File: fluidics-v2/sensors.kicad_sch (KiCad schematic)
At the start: 16 parts, among them IC6 HSCMAND060PA3A3, IC8 HSCMAND060PA3A3, J5 0533980671, U7 LTC4316CMS-TRPBF

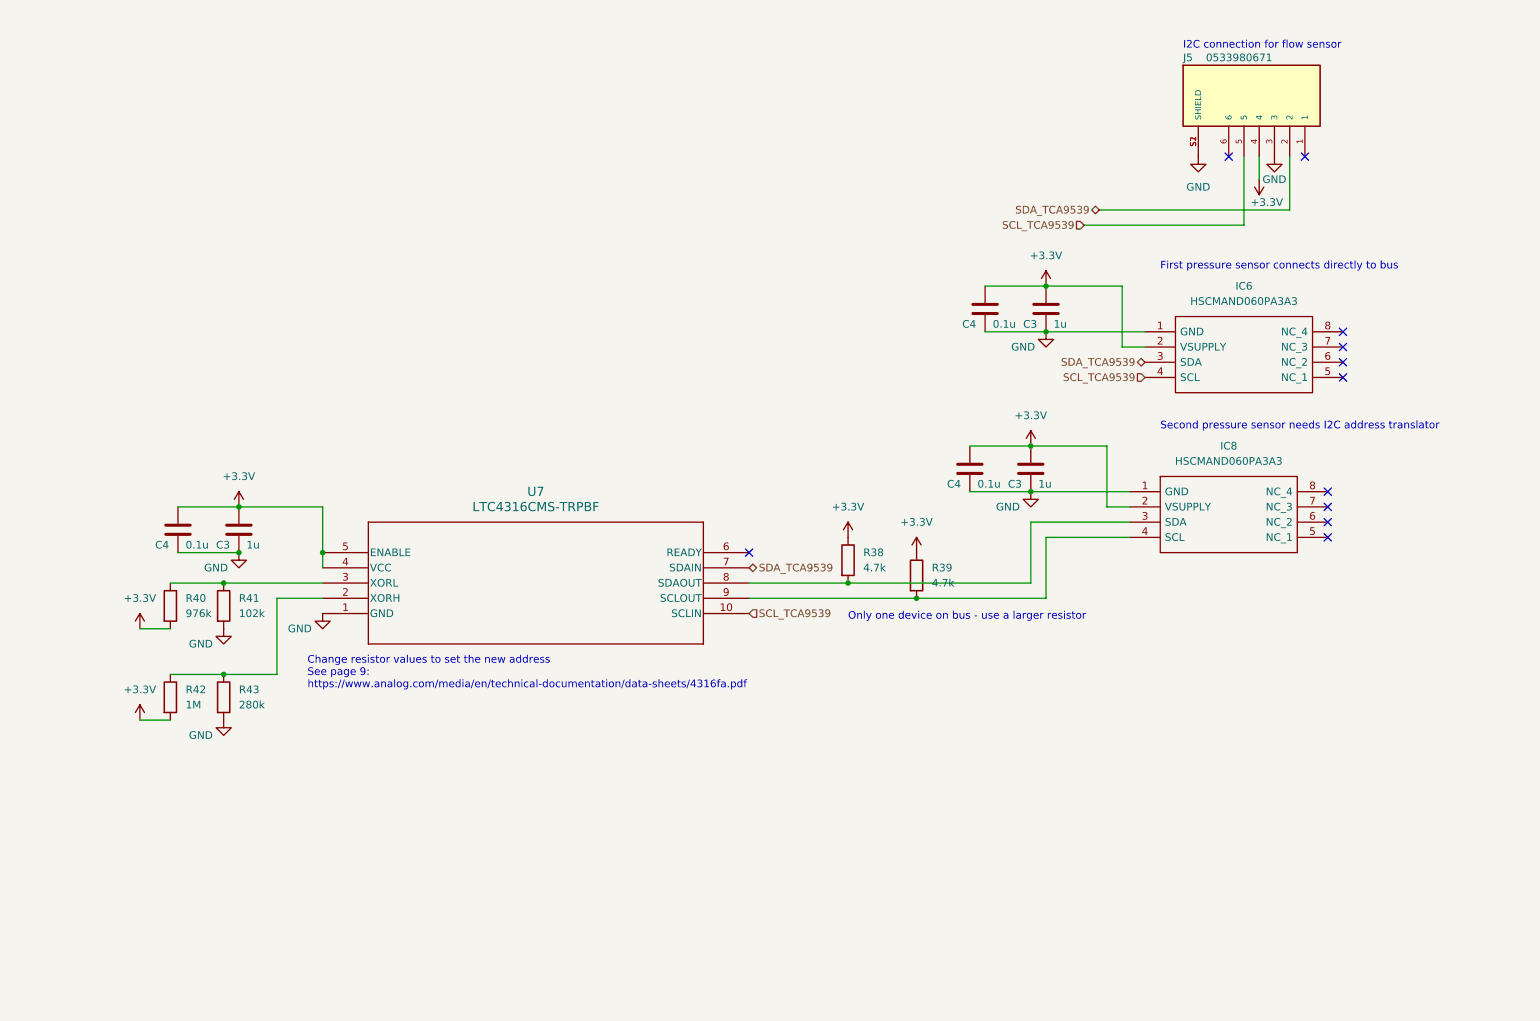
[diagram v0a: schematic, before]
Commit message: added footprints and mounting holes, cleaned up some sheets
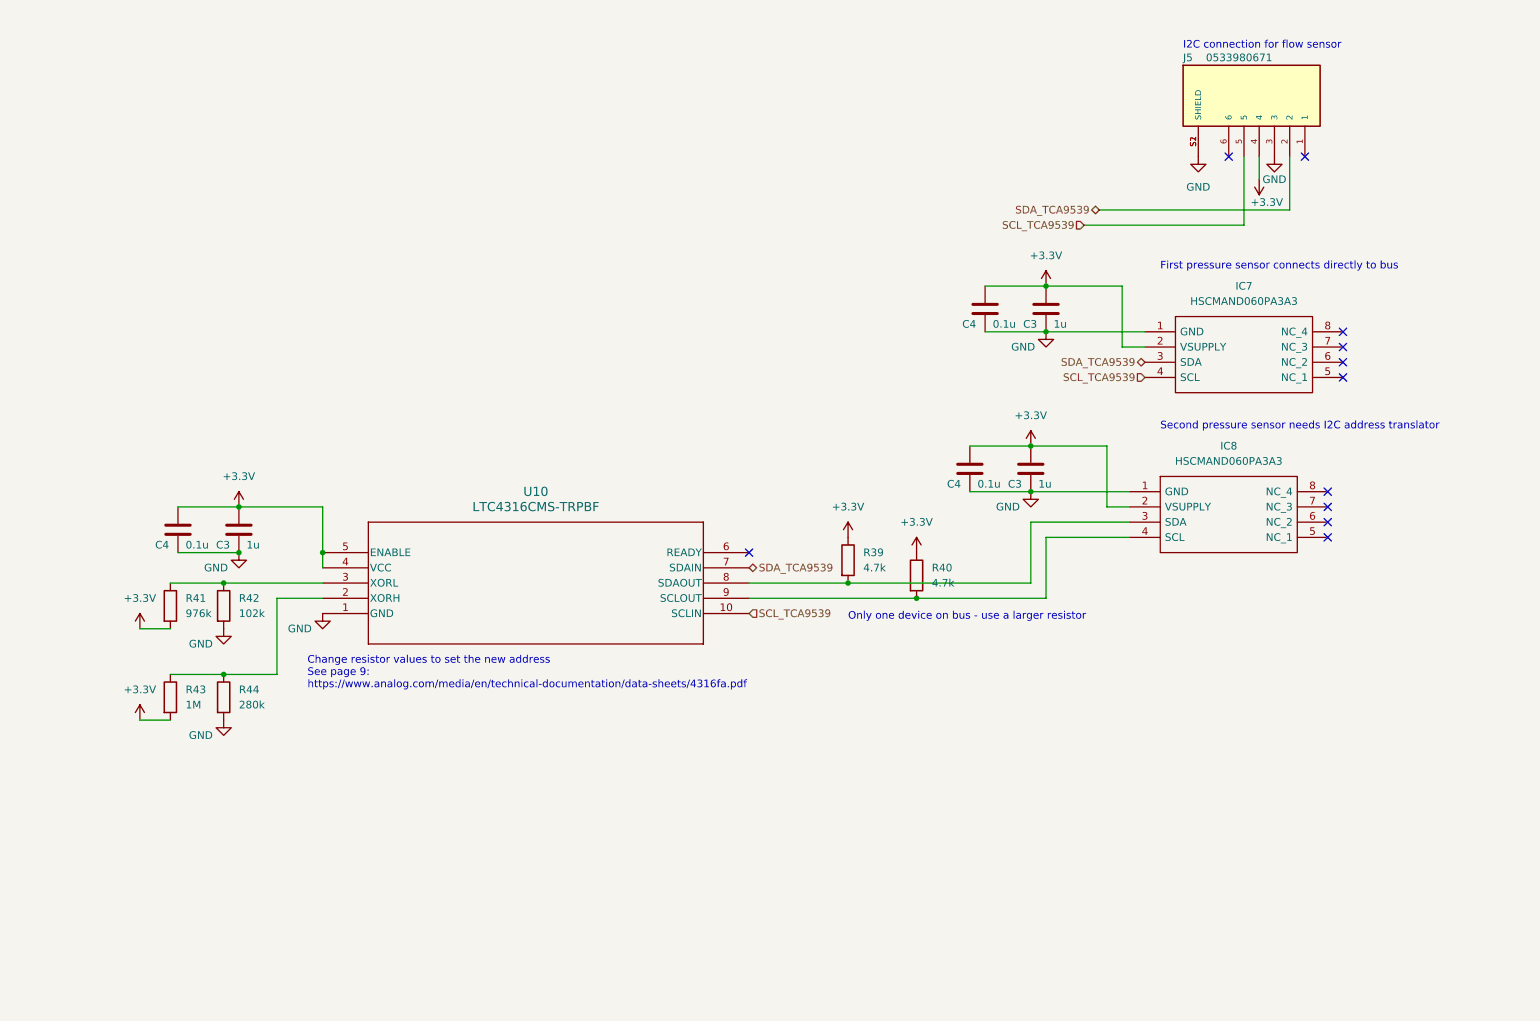
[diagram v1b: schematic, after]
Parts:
- renumbered IC6 to IC7, R38 to R39, R39 to R40, R40 to R41, R41 to R42, R42 to R43, R43 to R44, U7 to U10
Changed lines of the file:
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@@
         )
         (path "/0ec91c42-8aad-437d-8c85-5e10f0e51fe0/978ef52c-7a59-4000-92fc-4e58ca2b1aa7"
-          (reference "#PWR0131") (unit 1)
+          (reference "#PWR0139") (unit 1)
         )
       )
@@
         )
         (path "/0ec91c42-8aad-437d-8c85-5e10f0e51fe0/978ef52c-7a59-4000-92fc-4e58ca2b1aa7"
-          (reference "C37") (unit 1)
+          (reference "C41") (unit 1)
         )
       )
@@
   (symbol (lib_id "Device:R") (at 49.53 128.27 0) (unit 1)
     (in_bom yes) (on_board yes) (dnp no) (fields_autoplaced)
-    (property "Reference" "R41" (at 52.07 127 0)
+    (property "Reference" "R42" (at 52.07 127 0)
       (effects (font (size 1.27 1.27)) (justify left))
     )
@@
       (project "fluidics-v2"
         (path "/0ec91c42-8aad-437d-8c85-5e10f0e51fe0/978ef52c-7a59-4000-92fc-4e58ca2b1aa7"
-          (reference "R41") (unit 1)
+          (reference "R42") (unit 1)
         )
       )
@@
         )
         (path "/0ec91c42-8aad-437d-8c85-5e10f0e51fe0/978ef52c-7a59-4000-92fc-4e58ca2b1aa7"
-          (reference "#PWR0133") (unit 1)
+          (reference "#PWR0143") (unit 1)
         )
       )
@@
         )
         (path "/0ec91c42-8aad-437d-8c85-5e10f0e51fe0/978ef52c-7a59-4000-92fc-4e58ca2b1aa7"
-          (reference "#PWR0136") (unit 1)
+          (reference "#PWR0144") (unit 1)
         )
       )
@@
         )
         (path "/0ec91c42-8aad-437d-8c85-5e10f0e51fe0/978ef52c-7a59-4000-92fc-4e58ca2b1aa7"
-          (reference "#PWR0127") (unit 1)
+          (reference "#PWR0137") (unit 1)
         )
       )
@@
         )
         (path "/0ec91c42-8aad-437d-8c85-5e10f0e51fe0/978ef52c-7a59-4000-92fc-4e58ca2b1aa7"
-          (reference "C36") (unit 1)
+          (reference "C40") (unit 1)
         )
       )
@@
         )
         (path "/0ec91c42-8aad-437d-8c85-5e10f0e51fe0/978ef52c-7a59-4000-92fc-4e58ca2b1aa7"
-          (reference "#PWR0137") (unit 1)
+          (reference "#PWR0146") (unit 1)
         )
       )
@@
         )
         (path "/0ec91c42-8aad-437d-8c85-5e10f0e51fe0/978ef52c-7a59-4000-92fc-4e58ca2b1aa7"
-          (reference "C34") (unit 1)
+          (reference "C38") (unit 1)
         )
       )
@@
         )
         (path "/0ec91c42-8aad-437d-8c85-5e10f0e51fe0/978ef52c-7a59-4000-92fc-4e58ca2b1aa7"
-          (reference "#PWR0138") (unit 1)
+          (reference "#PWR0147") (unit 1)
         )
       )
@@
   (symbol (lib_id "Device:R") (at 153.67 120.65 0) (unit 1)
     (in_bom yes) (on_board yes) (dnp no) (fields_autoplaced)
-    (property "Reference" "R38" (at 156.21 119.38 0)
+    (property "Reference" "R39" (at 156.21 119.38 0)
       (effects (font (size 1.27 1.27)) (justify left))
     )
@@
       (project "fluidics-v2"
         (path "/0ec91c42-8aad-437d-8c85-5e10f0e51fe0/978ef52c-7a59-4000-92fc-4e58ca2b1aa7"
-          (reference "R38") (unit 1)
+          (reference "R39") (unit 1)
         )
       )
@@
         )
         (path "/0ec91c42-8aad-437d-8c85-5e10f0e51fe0/978ef52c-7a59-4000-92fc-4e58ca2b1aa7"
-          (reference "#PWR0134") (unit 1)
+          (reference "#PWR0140") (unit 1)
         )
       )
@@
         )
         (path "/0ec91c42-8aad-437d-8c85-5e10f0e51fe0/978ef52c-7a59-4000-92fc-4e58ca2b1aa7"
-          (reference "#PWR0135") (unit 1)
+          (reference "#PWR0142") (unit 1)
         )
       )
@@
         )
         (path "/0ec91c42-8aad-437d-8c85-5e10f0e51fe0/978ef52c-7a59-4000-92fc-4e58ca2b1aa7"
-          (reference "#PWR0132") (unit 1)
+          (reference "#PWR0141") (unit 1)
         )
       )
@@
   (symbol (lib_id "Device:R") (at 40.64 128.27 0) (unit 1)
     (in_bom yes) (on_board yes) (dnp no) (fields_autoplaced)
-    (property "Reference" "R40" (at 43.18 127 0)
+    (property "Reference" "R41" (at 43.18 127 0)
       (effects (font (size 1.27 1.27)) (justify left))
     )
@@
       (project "fluidics-v2"
         (path "/0ec91c42-8aad-437d-8c85-5e10f0e51fe0/978ef52c-7a59-4000-92fc-4e58ca2b1aa7"
-          (reference "R40") (unit 1)
+          (reference "R41") (unit 1)
         )
       )
@@
         )
         (path "/0ec91c42-8aad-437d-8c85-5e10f0e51fe0/978ef52c-7a59-4000-92fc-4e58ca2b1aa7"
-          (reference "C33") (unit 1)
+          (reference "C37") (unit 1)
         )
       )
@@
         )
         (path "/0ec91c42-8aad-437d-8c85-5e10f0e51fe0/978ef52c-7a59-4000-92fc-4e58ca2b1aa7"
-          (reference "#PWR0128") (unit 1)
+          (reference "#PWR0138") (unit 1)
         )
       )
@@
         )
         (path "/0ec91c42-8aad-437d-8c85-5e10f0e51fe0/978ef52c-7a59-4000-92fc-4e58ca2b1aa7"
-          (reference "C38") (unit 1)
+          (reference "C42") (unit 1)
         )
       )
@@
         )
         (path "/0ec91c42-8aad-437d-8c85-5e10f0e51fe0/978ef52c-7a59-4000-92fc-4e58ca2b1aa7"
-          (reference "#PWR010") (unit 1)
+          (reference "#PWR0134") (unit 1)
         )
       )
@@
   (symbol (lib_id "Device:R") (at 165.1 123.19 0) (unit 1)
     (in_bom yes) (on_board yes) (dnp no) (fields_autoplaced)
-    (property "Reference" "R39" (at 167.64 121.92 0)
+    (property "Reference" "R40" (at 167.64 121.92 0)
       (effects (font (size 1.27 1.27)) (justify left))
     )
@@
       (project "fluidics-v2"
         (path "/0ec91c42-8aad-437d-8c85-5e10f0e51fe0/978ef52c-7a59-4000-92fc-4e58ca2b1aa7"
-          (reference "R39") (unit 1)
+          (reference "R40") (unit 1)
         )
       )
@@
   (symbol (lib_id "Device:R") (at 40.64 143.51 0) (unit 1)
     (in_bom yes) (on_board yes) (dnp no) (fields_autoplaced)
-    (property "Reference" "R42" (at 43.18 142.24 0)
+    (property "Reference" "R43" (at 43.18 142.24 0)
       (effects (font (size 1.27 1.27)) (justify left))
     )
@@
       (project "fluidics-v2"
         (path "/0ec91c42-8aad-437d-8c85-5e10f0e51fe0/978ef52c-7a59-4000-92fc-4e58ca2b1aa7"
-          (reference "R42") (unit 1)
+          (reference "R43") (unit 1)
         )
       )
@@
         )
         (path "/0ec91c42-8aad-437d-8c85-5e10f0e51fe0/978ef52c-7a59-4000-92fc-4e58ca2b1aa7"
-          (reference "#PWR030") (unit 1)
+          (reference "#PWR0133") (unit 1)
         )
       )
@@
   (symbol (lib_id "LTC4316CMS:LTC4316CMS-TRPBF") (at 66.04 129.54 0) (mirror x) (unit 1)
     (in_bom yes) (on_board yes) (dnp no)
-    (property "Reference" "U7" (at 101.6 109.22 0)
+    (property "Reference" "U10" (at 101.6 109.22 0)
       (effects (font (size 1.524 1.524)))
     )
@@
       (project "fluidics-v2"
         (path "/0ec91c42-8aad-437d-8c85-5e10f0e51fe0/978ef52c-7a59-4000-92fc-4e58ca2b1aa7"
-          (reference "U7") (unit 1)
+          (reference "U10") (unit 1)
         )
       )
@@
         )
         (path "/0ec91c42-8aad-437d-8c85-5e10f0e51fe0/978ef52c-7a59-4000-92fc-4e58ca2b1aa7"
-          (reference "#PWR0125") (unit 1)
+          (reference "#PWR0135") (unit 1)
         )
       )
@@
   (symbol (lib_id "Device:R") (at 49.53 143.51 0) (unit 1)
     (in_bom yes) (on_board yes) (dnp no) (fields_autoplaced)
-    (property "Reference" "R43" (at 52.07 142.24 0)
+    (property "Reference" "R44" (at 52.07 142.24 0)
       (effects (font (size 1.27 1.27)) (justify left))
     )
@@
       (project "fluidics-v2"
         (path "/0ec91c42-8aad-437d-8c85-5e10f0e51fe0/978ef52c-7a59-4000-92fc-4e58ca2b1aa7"
-          (reference "R43") (unit 1)
+          (reference "R44") (unit 1)
         )
       )
@@
         )
         (path "/0ec91c42-8aad-437d-8c85-5e10f0e51fe0/978ef52c-7a59-4000-92fc-4e58ca2b1aa7"
-          (reference "C35") (unit 1)
+          (reference "C39") (unit 1)
         )
       )
@@
   (symbol (lib_id "honeywell:HSCMAND060PA3A3") (at 219.71 86.36 0) (unit 1)
     (in_bom yes) (on_board yes) (dnp no) (fields_autoplaced)
-    (property "Reference" "IC6" (at 219.71 74.93 0)
+    (property "Reference" "IC7" (at 219.71 74.93 0)
       (effects (font (size 1.27 1.27)))
     )
@@
       (project "fluidics-v2"
         (path "/0ec91c42-8aad-437d-8c85-5e10f0e51fe0/978ef52c-7a59-4000-92fc-4e58ca2b1aa7"
-          (reference "IC6") (unit 1)
+          (reference "IC7") (unit 1)
         )
       )
@@
         )
         (path "/0ec91c42-8aad-437d-8c85-5e10f0e51fe0/978ef52c-7a59-4000-92fc-4e58ca2b1aa7"
-          (reference "J5") (unit 1)
+          (reference "J16") (unit 1)
         )
       )
@@
         )
         (path "/0ec91c42-8aad-437d-8c85-5e10f0e51fe0/978ef52c-7a59-4000-92fc-4e58ca2b1aa7"
-          (reference "#PWR0126") (unit 1)
+          (reference "#PWR0136") (unit 1)
         )
       )
@@
         )
         (path "/0ec91c42-8aad-437d-8c85-5e10f0e51fe0/978ef52c-7a59-4000-92fc-4e58ca2b1aa7"
-          (reference "#PWR07") (unit 1)
+          (reference "#PWR0132") (unit 1)
         )
       )
@@
         )
         (path "/0ec91c42-8aad-437d-8c85-5e10f0e51fe0/978ef52c-7a59-4000-92fc-4e58ca2b1aa7"
-          (reference "#PWR0139") (unit 1)
-        )
-      )
+          (reference "#PWR0145") (unit 1)
+        )
+      )

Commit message: new version
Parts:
- removed C3 (x2): 1u, Capacitor_SMD:C_0603_1608Metric, symbol Device:C
- removed C4 (x2): 0.1u, Capacitor_SMD:C_0603_1608Metric, symbol Device:C
- removed IC7, IC8: HSCMAND060PA3A3, honeywell:HSCMRRN060MDSA3, symbol honeywell:HSCMAND060PA3A3
- removed J5: 0533980671, molex_connectors:MOLEX_0533980671, symbol 0533980671:0533980671
- added C3 (x4): 1u, Capacitor_SMD:C_0603_1608Metric, symbol Device:C
- added C4 (x4): 0.1u, Capacitor_SMD:C_0603_1608Metric, symbol Device:C
- added IC3, IC4, IC5, IC6: HSCDRRN001BDSA3, HSCDRRN001BDSA3, symbol HSCDRRN001BDSA3:HSCDRRN001BDSA3
- R43: value 1M -> DNP
- R44: value 280k -> 0
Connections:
- net +3.3V: now also C3.1, C3.1, C3.1, C3.1, C4.1, C4.1, C4.1, C4.1, IC3.2 (VSUPPLY), IC4.2 (VSUPPLY), IC5.2 (VSUPPLY), IC6.2 (VSUPPLY)
- net GND: now also C3.2, C3.2, C3.2, C3.2, C4.2, C4.2, C4.2, C4.2, IC3.1 (GND), IC4.1 (GND), IC5.1 (GND), IC6.1 (GND)
- net SDA_OUT: now reaches R39.2, U10.8 (SDAOUT)
- net SCL_OUT: now reaches R40.2, U10.9 (SCLOUT)
- net SCL_TCA9539 renamed SCL_IN
- net SDA_TCA9539 renamed SDA_IN
- new net MISO: IC3.3 (MISO), IC4.3 (MISO), IC5.3 (MISO), IC6.3 (MISO)
- new net SCK: IC3.4 (SCLK), IC4.4 (SCLK), IC5.4 (SCLK), IC6.4 (SCLK)
- new net ~{CS}0: IC3.5 (SS)
- new net ~{CS}1: IC4.5 (SS)
- new net ~{CS}2: IC5.5 (SS)
- new net ~{CS}3: IC6.5 (SS)
- no-connect marks 11 -> 13
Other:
- note added: "Address translator for second flow sensor"
- note removed: "First pressure sensor connects directly to bus"
- note removed: "I2C connection for flow sensor"
- note removed: "Second pressure sensor needs I2C address translator"
- moved on the sheet: C3, C4, R39, R40, R41, R42, R43, R44, U10

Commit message: started layout
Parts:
- IC3, IC4, IC5, IC6: footprint HSCDRRN001BDSA3 -> HSCDRRN001BDSA3:HSCDRRN001BDSA3
- renumbered C4 to C?, C3 to C?, R43 to R42, R42 to R43, R39 to R45, R40 to R46, U10 to U12
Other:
- note added: "Address translator for second flow sensor - DNP if using only one"
- note added: "Pressure sensors connect over SPI and have unique chip select pins"
- note removed: "Address translator for second flow sensor"
- moved on the sheet: C?, IC3
